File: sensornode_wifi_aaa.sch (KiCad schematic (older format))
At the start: 34 parts, among them K1 ICSP, K2 USB, K3 AD-HOC, K4 T2, K5 T1, SW1 uC_RESET, SW2 WiFi_RESET, U1 MCP1640, U2 PIC18F2XJ53, U3 RN-171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

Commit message: new layout, changed connectors to 0.1in
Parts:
- removed K4: T2, symbol CONN_3
- removed K5: T1, symbol CONN_3
- removed R10: 4.7K, symbol R
- added D1: LED, symbol LED
- added P1: CONN_14, symbol CONN_14
- added R?: R, symbol R
- added SW3: CMD, symbol SW_PUSH
- R9: value 4.7K -> 10K
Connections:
- net +3.3V: now also R9.1, P1.1 (P1), P1.10 (P10), P1.4 (P4), P1.7 (P7), R?.1; no longer R9.2
- net GND: now also P1.12 (P12), P1.14 (P14), P1.3 (P3), P1.6 (P6), P1.9 (P9), SW3.1
- net RA0: now also R9.2, SW3.2
- net RA1: now also D1.2 (K)
- net RB0: now also P1.2 (P2); no longer R9.1
- net RB1: now also P1.5 (P5)
- net RB2: now also P1.8 (P8)
- net RB3: now also P1.11 (P11)
- net RB4: now also P1.13 (P13)
- net RB5: now also SW2.2, U3.40 (!RESET)
- new net: D1.1 (A), R?.2

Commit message: before removing USB
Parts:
- removed BT1: BATTERY_MID, symbol BATTERY_MID
- added BT1, BT2: BATTERY, symbol BATTERY
- added P2: CONN_14, symbol CONN_14
- gave numbers to parts that had none: 1
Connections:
- net +3.3V: now also P2.1 (P1), P2.10 (P10), P2.4 (P4), P2.7 (P7)
- net GND: now also BT2.2 (-), P2.12 (P12), P2.13 (P13), P2.14 (P14), P2.3 (P3), P2.6 (P6), P2.9 (P9)
- net RA0: now also P2.2 (P2)
- net RA1: now also P2.5 (P5)
- net RA2: now also P2.11 (P11)
- net RA3: now also P2.8 (P8)
- net at C1.1, L1.1, U1.3 (EN)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: now also BT1.1 (+)
- new net: BT1.2 (-), BT2.1 (+)
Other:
- moved on the sheet: D1, P1, R10, R9, SW3

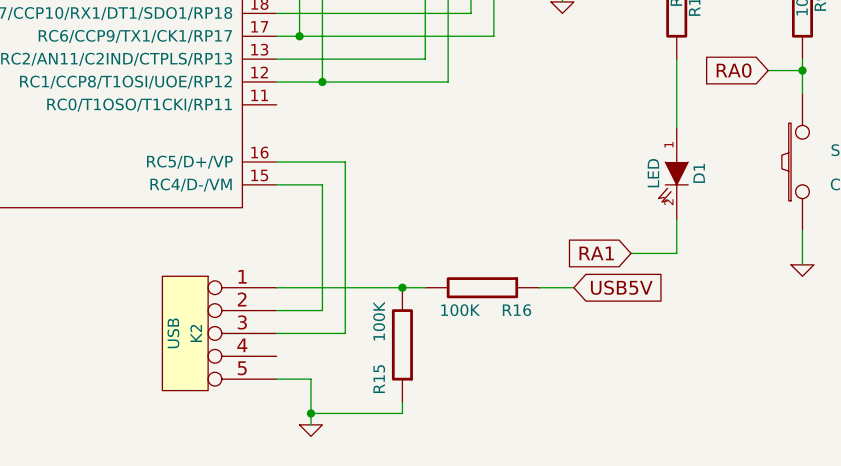
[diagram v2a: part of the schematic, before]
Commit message: Changed to AA batteries
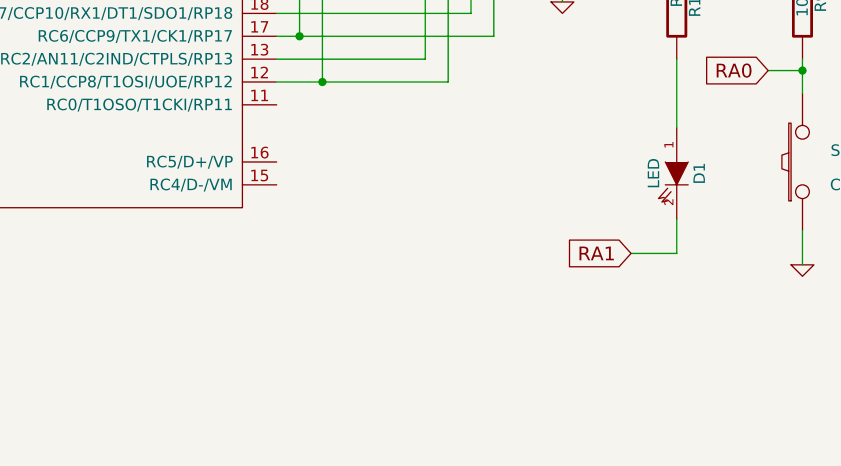
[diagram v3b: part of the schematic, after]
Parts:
- removed K2: USB, symbol CONN_5
- removed R15, R16: 100K, symbol R
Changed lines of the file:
@@
-EESchema Schematic File Version 2  date Sun 27 Jan 2013 14:10:16 CET
+EESchema Schematic File Version 2  date Sat 09 Feb 2013 14:20:02 CET
 LIBS:power
 LIBS:device
@@
 	1700 6250 2550 6250
 Wire Wire Line
-	7050 6900 6900 6900
-Connection ~ 5900 7450
-Wire Wire Line
-	5900 7450 6300 7450
-Wire Wire Line
-	6300 7450 6300 7400
-Wire Wire Line
 	5750 4400 6050 4400
 Wire Wire Line
 	5750 4200 6050 4200
-Wire Wire Line
-	5750 7100 6050 7100
-Wire Wire Line
-	6050 7100 6050 6350
-Wire Wire Line
-	6050 6350 5750 6350
-Wire Wire Line
-	5900 7500 5900 7300
-Wire Wire Line
-	5900 7300 5750 7300
 Wire Wire Line
 	4550 1850 4450 1850
@@
 	4500 1650 4500 2000
 Wire Wire Line
-	5750 7000 5950 7000
-Wire Wire Line
-	5950 7000 5950 6450
-Wire Wire Line
-	5950 6450 5750 6450
-Wire Wire Line
 	6050 4100 5750 4100
 Wire Wire Line
 	6050 4300 5750 4300
-Wire Wire Line
-	6400 6900 5750 6900
-Connection ~ 6300 6900
 Wire Wire Line
 	2550 6400 2500 6400
@@
 	1    2500 7200
 	1    0    0    -1
-$EndComp
-Text GLabel 7050 6900 2    60   Input ~ 0
-USB5V
-$Comp
-L R R16
-U 1 1 4FF099B1
-P 6650 6900
-F 0 "R16" V 6750 7050 50  0000 C CNN
-F 1 "100K" V 6750 6800 50  0000 C CNN
-	1    6650 6900
-	0    1    1    0
-$EndComp
-$Comp
-L R R15
-U 1 1 4FF099A8
-P 6300 7150
-F 0 "R15" V 6400 7300 50  0000 C CNN
-F 1 "100K" V 6400 7050 50  0000 C CNN
-	1    6300 7150
-	-1   0    0    1
 $EndComp
 Text GLabel 6050 4400 2    60   Input ~ 0
@@
 	1    0    0    -1
 $EndComp
-$Comp
-L CONN_5 K2
-U 1 1 4FEDDEA8
-P 5350 7100
-F 0 "K2" V 5300 7100 50  0000 C CNN
-F 1 "USB" V 5400 7100 50  0000 C CNN
-	1    5350 7100
-	-1   0    0    -1
-$EndComp
 Text GLabel 2350 3800 0    60   Input ~ 0
 MCLR
@@
 Text GLabel 4450 1850 0    60   Input ~ 0
 RB6
-$Comp
-L GND #PWR027
-U 1 1 4FEDDEA6
-P 5900 7500
-F 0 "#PWR027" H 5900 7500 30  0001 C CNN
-F 1 "GND" H 5900 7430 30  0001 C CNN
-	1    5900 7500
-	1    0    0    -1
-$EndComp
 Text Label 8300 2050 0    60   ~ 0
 antenna
@@
 $EndComp
 $Comp
-L +3.3V #PWR028
+L +3.3V #PWR027
 U 1 1 4FEDDEA1
 P 9950 3000
-F 0 "#PWR028" H 9950 2960 30  0001 C CNN
+F 0 "#PWR027" H 9950 2960 30  0001 C CNN
 F 1 "+3.3V" H 9950 3100 30  0000 C CNN
 	1    9950 3000
@@
 $EndComp
 $Comp
-L GND #PWR029
+L GND #PWR028
 U 1 1 4FEDDEA0
 P 9950 3650
-F 0 "#PWR029" H 9950 3650 30  0001 C CNN
+F 0 "#PWR028" H 9950 3650 30  0001 C CNN
 F 1 "GND" H 9950 3580 30  0001 C CNN
 	1    9950 3650
